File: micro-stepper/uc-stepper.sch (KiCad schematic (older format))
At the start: 30 parts, among them P1 CONN_8, P2 CONN_2, P3 ICSP, P4 CONN_6, P5 CONN_2, P6 CONN_2, P7 CONN_2, U1 16F1507

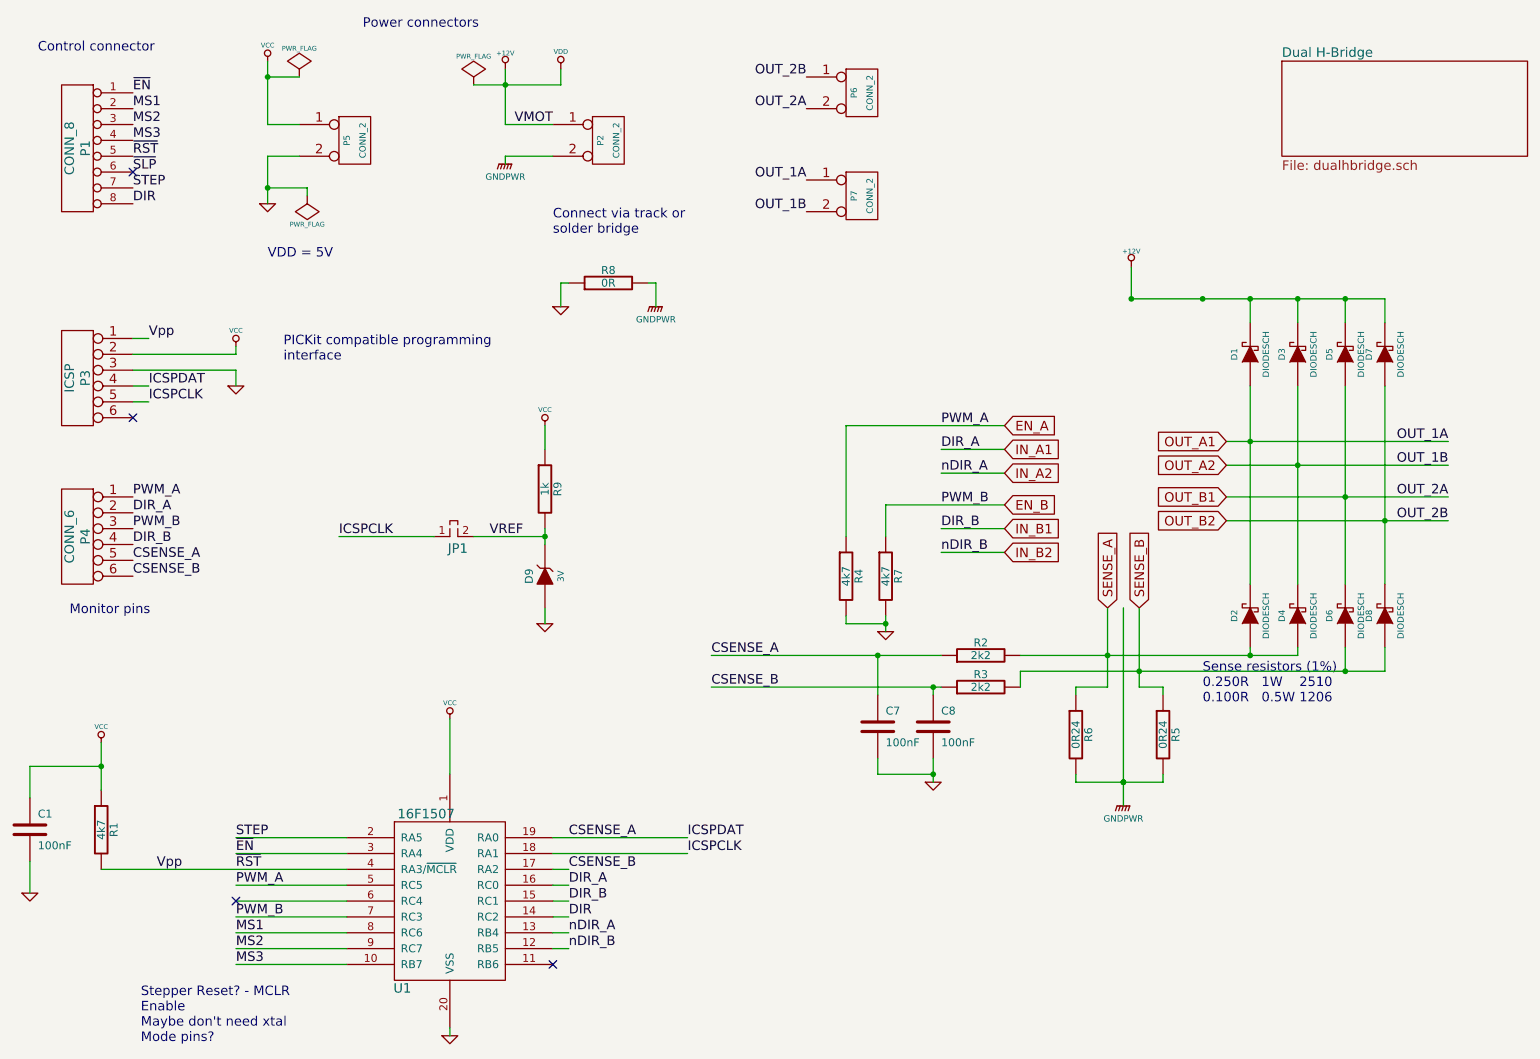
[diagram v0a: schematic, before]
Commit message: Update schematic, PCB
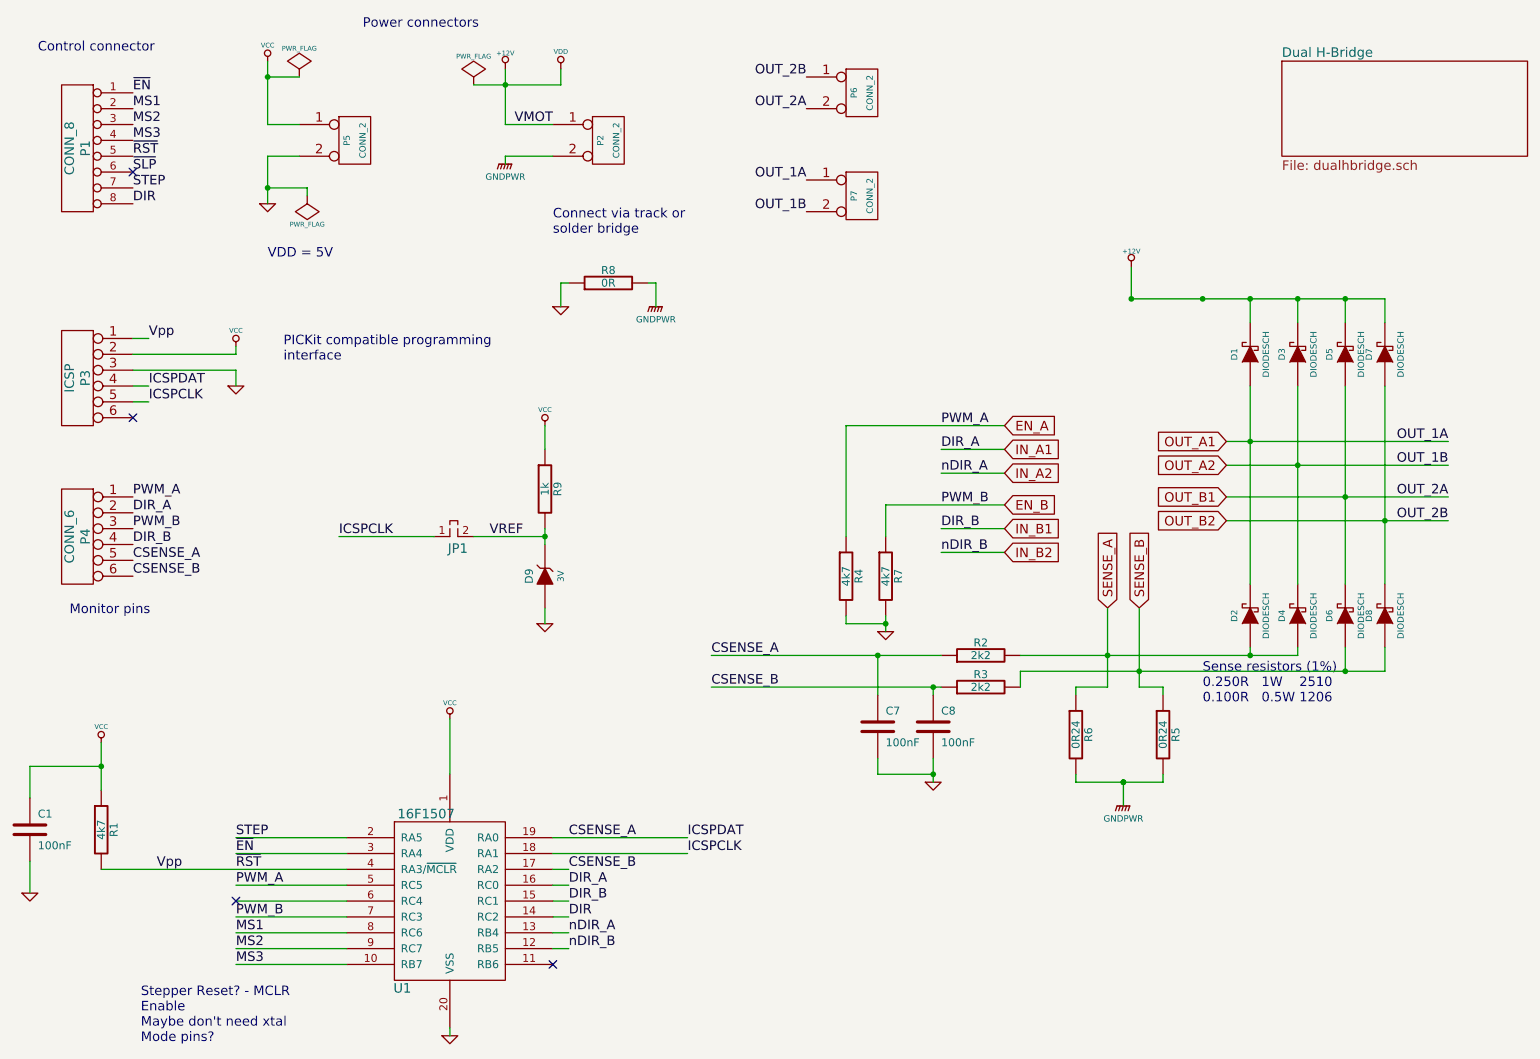
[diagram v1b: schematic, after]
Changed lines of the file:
@@
-EESchema Schematic File Version 2  date 23/09/2012 21:46:17
+EESchema Schematic File Version 2  date 24/09/2012 01:49:36
 LIBS:power
 LIBS:device
@@
 $EndDescr
 Wire Wire Line
-	7600 2200 7600 2400
-Wire Wire Line
-	6800 3700 6050 3700
-Wire Wire Line
-	6050 3700 6050 3900
+	7550 5450 7550 5600
+Wire Wire Line
+	3450 1050 4000 1050
+Wire Wire Line
+	4000 1050 4000 950
+Wire Wire Line
+	3900 4450 3900 4350
+Wire Wire Line
+	3450 3900 3900 3900
+Wire Wire Line
+	3900 3200 3900 3350
+Wire Wire Line
+	7800 4900 7800 4850
+Wire Wire Line
+	7800 4850 7650 4850
+Wire Wire Line
+	7450 4850 7250 4850
+Wire Wire Line
+	6800 3200 5800 3200
+Wire Wire Line
+	5800 3200 5800 3900
+Connection ~ 6050 4450
+Wire Wire Line
+	6050 4450 5800 4450
+Wire Wire Line
+	5800 4450 5800 4400
+Wire Wire Line
+	1950 6600 2650 6600
+Wire Wire Line
+	2650 6400 1950 6400
+Wire Wire Line
+	4050 6400 3950 6400
+Wire Wire Line
+	6800 3350 6400 3350
+Wire Wire Line
+	6800 3850 6400 3850
+Wire Wire Line
+	2150 1800 2150 1500
+Wire Wire Line
+	4000 2450 4000 2300
+Wire Wire Line
+	4000 2300 4050 2300
+Wire Wire Line
+	7250 5400 7250 5450
+Wire Wire Line
+	1950 5900 2650 5900
+Wire Wire Line
+	4800 5900 3950 5900
+Wire Wire Line
+	1400 3050 1300 3050
+Wire Wire Line
+	1400 2650 1300 2650
+Wire Wire Line
+	1950 2700 1950 2750
+Wire Wire Line
+	1950 2750 1300 2750
+Connection ~ 2150 1000
+Wire Wire Line
+	2350 1000 2150 1000
+Wire Wire Line
+	3950 6200 4050 6200
+Wire Wire Line
+	4050 6100 3950 6100
+Wire Wire Line
+	1950 6300 2650 6300
+Wire Wire Line
+	3300 5050 3300 5400
+Wire Wire Line
+	650  6150 650  5950
+Wire Wire Line
+	650  5550 650  5350
+Wire Wire Line
+	650  5350 1100 5350
+Connection ~ 6350 4850
+Wire Wire Line
+	6400 4850 4950 4850
+Wire Wire Line
+	6350 5450 6350 5300
+Wire Wire Line
+	6350 4900 6350 4850
+Wire Wire Line
+	6900 4650 8650 4650
+Wire Wire Line
+	9200 4600 9200 4750
+Connection ~ 8350 4650
+Wire Wire Line
+	8650 4650 8650 4600
+Wire Wire Line
+	9200 2950 9200 4200
+Wire Wire Line
+	8650 2950 8650 4200
+Connection ~ 9200 3800
+Connection ~ 8650 3450
+Connection ~ 8650 2400
+Wire Wire Line
+	8950 2400 8950 2550
+Connection ~ 7600 2400
+Wire Wire Line
+	8350 2400 8350 2550
+Wire Wire Line
+	8200 3800 9600 3800
+Wire Wire Line
+	8200 3450 9600 3450
+Wire Wire Line
+	7650 4850 7650 4350
+Connection ~ 7550 5450
+Connection ~ 1100 5350
+Wire Wire Line
+	1100 5500 1100 5200
+Wire Wire Line
+	2150 900  2150 1300
+Wire Wire Line
+	2150 1300 2350 1300
+Wire Wire Line
+	2150 1500 2350 1500
+Wire Wire Line
+	3950 1500 3650 1500
+Wire Wire Line
+	3650 950  3650 1300
+Wire Wire Line
+	2650 6000 1100 6000
+Connection ~ 7550 5450
+Wire Wire Line
+	7450 4850 7450 4350
+Wire Wire Line
+	8200 3650 9600 3650
+Connection ~ 8350 3300
+Wire Wire Line
+	8650 2400 8650 2550
+Connection ~ 8350 2400
+Wire Wire Line
+	9200 2400 7600 2400
+Wire Wire Line
+	9200 2400 9200 2550
+Connection ~ 8950 2400
+Connection ~ 8950 3650
+Wire Wire Line
+	8350 2950 8350 4200
+Wire Wire Line
+	8950 2950 8950 4200
+Wire Wire Line
+	9600 3300 8200 3300
+Wire Wire Line
+	8350 4600 8350 4650
+Connection ~ 7450 4650
+Wire Wire Line
+	8950 4600 8950 4750
+Connection ~ 7650 4750
+Connection ~ 8950 4750
+Connection ~ 8050 2400
+Wire Wire Line
+	9200 4750 6900 4750
+Wire Wire Line
+	6900 4750 6900 4850
+Wire Wire Line
+	6000 4900 6000 4650
+Wire Wire Line
+	6400 4650 4950 4650
+Connection ~ 6000 4650
+Wire Wire Line
+	6000 5300 6000 5400
+Wire Wire Line
+	6000 5400 6350 5400
+Connection ~ 6350 5400
+Wire Wire Line
+	2650 6100 1950 6100
+Wire Wire Line
+	3950 6000 4050 6000
+Wire Wire Line
+	4050 6300 3950 6300
+Wire Wire Line
+	3650 1300 3950 1300
+Connection ~ 3650 1050
+Wire Wire Line
+	2400 1750 2400 1700
+Wire Wire Line
+	2400 1700 2150 1700
+Connection ~ 2150 1700
+Wire Wire Line
+	1300 2850 1950 2850
+Wire Wire Line
+	1950 2850 1950 2950
+Wire Wire Line
+	1400 2950 1300 2950
+Wire Wire Line
+	4800 5800 3950 5800
+Wire Wire Line
+	1950 6200 2650 6200
+Wire Wire Line
+	2650 5800 1950 5800
+Wire Wire Line
+	7250 4850 7250 4900
+Wire Wire Line
+	4550 2300 4600 2300
+Wire Wire Line
+	4600 2300 4600 2450
+Wire Wire Line
+	3650 1500 3650 1550
+Wire Wire Line
+	6400 4000 6800 4000
+Wire Wire Line
+	6400 3500 6800 3500
+Wire Wire Line
+	3300 7000 3300 7050
+Wire Wire Line
+	3950 6500 4050 6500
+Wire Wire Line
+	2650 6500 1950 6500
+Wire Wire Line
+	6050 4400 6050 4500
+Wire Wire Line
+	2600 3900 3200 3900
+Wire Wire Line
+	7800 5400 7800 5450
+Wire Wire Line
+	7800 5450 7250 5450
+Wire Wire Line
+	3900 3850 3900 3950
 Connection ~ 3900 3900
 Wire Wire Line
-	3900 3850 3900 3950
-Wire Wire Line
-	7800 5450 7250 5450
-Wire Wire Line
-	7800 5450 7800 5400
-Wire Wire Line
-	2600 3900 3200 3900
-Wire Wire Line
-	6050 4400 6050 4500
-Wire Wire Line
-	2650 6500 1950 6500
-Wire Wire Line
-	3950 6500 4050 6500
-Wire Wire Line
-	3300 7000 3300 7050
-Wire Wire Line
-	6400 3500 6800 3500
-Wire Wire Line
-	6400 4000 6800 4000
-Wire Wire Line
-	3650 1550 3650 1500
-Wire Wire Line
-	4600 2450 4600 2300
-Wire Wire Line
-	4600 2300 4550 2300
-Wire Wire Line
-	7250 4900 7250 4850
-Wire Wire Line
-	2650 5800 1950 5800
-Wire Wire Line
-	1950 6200 2650 6200
-Wire Wire Line
-	4800 5800 3950 5800
-Wire Wire Line
-	1400 2950 1300 2950
-Wire Wire Line
-	1950 2950 1950 2850
-Wire Wire Line
-	1950 2850 1300 2850
-Connection ~ 2150 1700
-Wire Wire Line
-	2150 1700 2400 1700
-Wire Wire Line
-	2400 1700 2400 1750
-Connection ~ 3650 1050
-Wire Wire Line
-	3950 1300 3650 1300
-Wire Wire Line
-	4050 6300 3950 6300
-Wire Wire Line
-	3950 6000 4050 6000
-Wire Wire Line
-	2650 6100 1950 6100
-Connection ~ 6350 5400
-Wire Wire Line
-	6350 5400 6000 5400
-Wire Wire Line
-	6000 5400 6000 5300
-Connection ~ 6000 4650
-Wire Wire Line
-	6400 4650 4950 4650
-Wire Wire Line
-	6000 4900 6000 4650
-Wire Wire Line
-	6900 4850 6900 4750
-Wire Wire Line
-	6900 4750 9200 4750
-Connection ~ 8050 2400
-Connection ~ 8950 4750
-Connection ~ 7650 4750
-Wire Wire Line
-	8950 4600 8950 4750
-Connection ~ 7450 4650
-Wire Wire Line
-	8350 4600 8350 4650
-Wire Wire Line
-	9600 3300 8200 3300
-Wire Wire Line
-	8950 2950 8950 4200
-Wire Wire Line
-	8350 2950 8350 4200
-Connection ~ 8950 3650
-Connection ~ 8950 2400
-Wire Wire Line
-	9200 2550 9200 2400
-Wire Wire Line
-	9200 2400 7600 2400
-Connection ~ 8350 2400
-Wire Wire Line
-	8650 2400 8650 2550
-Connection ~ 8350 3300
-Wire Wire Line
-	8200 3650 9600 3650
-Wire Wire Line
-	7450 4350 7450 4850
-Connection ~ 7550 5450
-Wire Wire Line
-	2650 6000 1100 6000
-Wire Wire Line
-	3650 1300 3650 950
-Wire Wire Line
-	3650 1500 3950 1500
-Wire Wire Line
-	2350 1500 2150 1500
-Wire Wire Line
-	2350 1300 2150 1300
-Wire Wire Line
-	2150 1300 2150 900
-Wire Wire Line
-	1100 5500 1100 5200
-Connection ~ 1100 5350
-Connection ~ 7550 5450
-Wire Wire Line
-	7650 4350 7650 4850
-Wire Wire Line
-	8200 3450 9600 3450
-Wire Wire Line
-	8200 3800 9600 3800
-Wire Wire Line
-	8350 2400 8350 2550
-Connection ~ 7600 2400
-Wire Wire Line
-	8950 2400 8950 2550
-Connection ~ 8650 2400
-Connection ~ 8650 3450
-Connection ~ 9200 3800
-Wire Wire Line
-	8650 2950 8650 4200
-Wire Wire Line
-	9200 2950 9200 4200
-Wire Wire Line
-	7550 5600 7550 4350
-Wire Wire Line
-	8650 4600 8650 4650
-Connection ~ 8350 4650
-Wire Wire Line
-	9200 4750 9200 4600
-Wire Wire Line
-	8650 4650 6900 4650
-Wire Wire Line
-	6350 4900 6350 4850
-Wire Wire Line
-	6350 5450 6350 5300
-Wire Wire Line
-	6400 4850 4950 4850
-Connection ~ 6350 4850
-Wire Wire Line
-	1100 5350 650  5350
-Wire Wire Line
-	650  5350 650  5550
-Wire Wire Line
-	650  6150 650  5950
-Wire Wire Line
-	3300 5050 3300 5400
-Wire Wire Line
-	1950 6300 2650 6300
-Wire Wire Line
-	4050 6100 3950 6100
-Wire Wire Line
-	3950 6200 4050 6200
-Wire Wire Line
-	2350 1000 2150 1000
-Connection ~ 2150 1000
-Wire Wire Line
-	1300 2750 1950 2750
-Wire Wire Line
-	1950 2750 1950 2700
-Wire Wire Line
-	1400 2650 1300 2650
-Wire Wire Line
-	1400 3050 1300 3050
-Wire Wire Line
-	4800 5900 3950 5900
-Wire Wire Line
-	1950 5900 2650 5900
-Wire Wire Line
-	7250 5450 7250 5400
-Wire Wire Line
-	4050 2300 4000 2300
-Wire Wire Line
-	4000 2300 4000 2450
-Wire Wire Line
-	2150 1500 2150 1800
-Wire Wire Line
-	6800 3850 6400 3850
-Wire Wire Line
-	6800 3350 6400 3350
-Wire Wire Line
-	4050 6400 3950 6400
-Wire Wire Line
-	2650 6400 1950 6400
-Wire Wire Line
-	1950 6600 2650 6600
-Wire Wire Line
-	5800 4400 5800 4450
-Wire Wire Line
-	5800 4450 6050 4450
-Connection ~ 6050 4450
-Wire Wire Line
-	5800 3900 5800 3200
-Wire Wire Line
-	5800 3200 6800 3200
-Wire Wire Line
-	7450 4850 7250 4850
-Wire Wire Line
-	7650 4850 7800 4850
-Wire Wire Line
-	7800 4850 7800 4900
-Wire Wire Line
-	3900 3200 3900 3350
-Wire Wire Line
-	3450 3900 3900 3900
-Wire Wire Line
-	3900 4450 3900 4350
-Wire Wire Line
-	4000 950  4000 1050
-Wire Wire Line
-	4000 1050 3450 1050
+	6050 3900 6050 3700
+Wire Wire Line
+	6050 3700 6800 3700
+Wire Wire Line
+	7600 2400 7600 2200
 $Comp
 L VDD #PWR01

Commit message: Update gate drive on P-FETS; remove external diodes
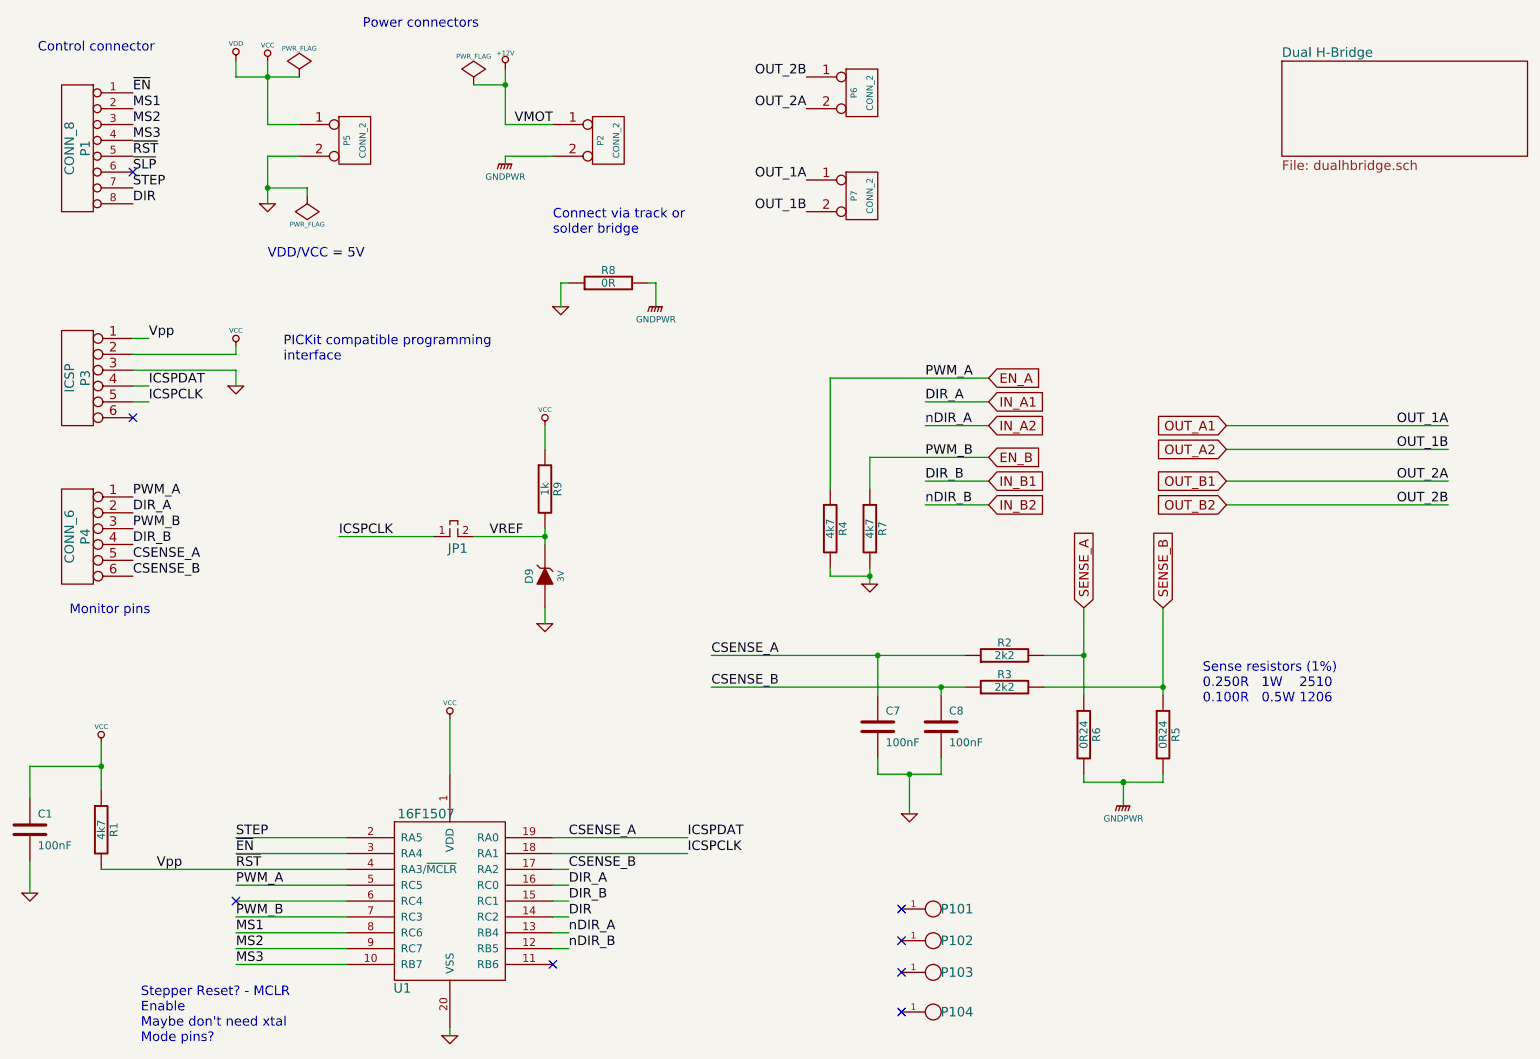
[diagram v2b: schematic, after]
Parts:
- removed D1, D2, D3, D4, D5, D6, D7, D8: DIODESCH, symbol DIODESCH
- added P101, P102, P103, P104: 1PIN_TH, symbol 1PIN_TH
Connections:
- no-connect marks 4 -> 8
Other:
- note added: "VDD/VCC = 5V"
- note removed: "VDD = 5V"
- moved on the sheet: C8, R2, R3, R4, R6, R7
